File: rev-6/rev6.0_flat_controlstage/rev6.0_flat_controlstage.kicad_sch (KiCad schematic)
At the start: 103 parts, among them J1 PROG, J2 COMM, J3 OSCOPE, J4 PHASE_SIG, J5 ENC_SIG, J6 ANALOG_SIG, J7 POWER, J8 LED, U1 TPS62112, U2 STM32G474RBTx, U3 NCP115ASN330T2G, U4 LM4040C30FTA, U5 LP5900SD-3.3/NOPB, U6 TCAN330, U7 LMV831, Y1 Crystal_GND24

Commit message: Rev 6 pre design review
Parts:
- removed J8: LED, Connector_PinHeader_2.54mm:PinHeader_1x04_P2.54mm_Horizontal, symbol Connector_Generic:Conn_01x04
- removed NT2: NetTie_2, NetTie:NetTie-2_SMD_Pad0.5mm, symbol Device:NetTie_2
- added C52: DNP, Capacitor_SMD:C_0603_1608Metric, symbol Device:C_Small
- added R27, R28: 0, Resistor_SMD:R_0603_1608Metric, symbol Device:R_Small_US
- added TP1, TP10, TP11, TP12, TP13, TP14, TP15, TP16, TP17, TP18, TP19, TP2, TP20, TP21, TP22, TP23, TP24, TP25, TP26, TP27, TP28, TP29, TP3, TP30, TP31, TP4, TP5, TP6, TP7, TP8, TP9: TestPoint_Small, project-footprints:TestPoint_Keystone_5015_Micro-Minature_3DMODEL, symbol Connector:TestPoint_Small
- C12, C13, C14, C16, C17, C18, C20, C22, C23, C25, C27, C28, C31, C32, C34, C44, C45, C46, C48: footprint Capacitor_SMD:C_0603_1608Metric -> Capacitor_SMD:C_0402_1005Metric
- D2, D3, D4: footprint LED_SMD:LED-APA102-2020 -> project-footprints:APA102_2020
- J4: footprint Connector_PinHeader_2.54mm:PinHeader_1x10_P2.54mm_Horizontal -> Connector_PinHeader_2.54mm:PinHeader_2x07_P2.54mm_Horizontal; symbol Connector_Generic:Conn_01x10 -> Connector_Generic:Conn_02x07_Odd_Even
- J5: footprint Connector_PinHeader_2.54mm:PinHeader_1x09_P2.54mm_Horizontal -> Connector_PinHeader_2.54mm:PinHeader_2x06_P2.54mm_Horizontal; symbol Connector_Generic:Conn_01x09 -> Connector_Generic:Conn_02x06_Odd_Even
- J7: footprint Connector_PinHeader_2.54mm:PinHeader_1x03_P2.54mm_Horizontal -> Connector_PinHeader_2.54mm:PinHeader_1x02_P2.54mm_Horizontal; symbol Connector_Generic:Conn_01x03 -> Connector_Generic:Conn_01x02
- R10, R15, R16, R17, R18, R19, R20, R21, R22, R4, R5, R6, R7, R9: footprint Resistor_SMD:R_0603_1608Metric -> Resistor_SMD:R_0402_1005Metric
- R13: value 35.7k -> 35.7k/0.1%
- R14: value 10.2k -> 10.2k/0.1%
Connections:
- net +3V0: now also TP9.1
- net +3V3: now also TP11.1
- net +3V3A: now also TP24.1
- net +5V: now also TP7.1
- net ENC_A: now also J5.3 (Pin_3), TP5.1; no longer J5.2 (Pin_2)
- net ENC_B: now also J5.4 (Pin_4), TP6.1; no longer J5.3 (Pin_3)
- net GND: now also J4.13 (Pin_13), J4.14 (Pin_14), J4.2 (Pin_2), J4.5 (Pin_5), J4.6 (Pin_6), J4.9 (Pin_9), J5.11 (Pin_11), J5.12 (Pin_12), J5.2 (Pin_2), J5.5 (Pin_5), J5.6 (Pin_6), J7.2 (Pin_2), R27.1, TP10.1, TP12.1, TP14.1, TP2.1, TP27.1, TP28.1, TP29.1, TP30.1, TP8.1; no longer J4.4 (Pin_4), J4.7 (Pin_7), J5.4 (Pin_4), J5.9 (Pin_9), J7.1 (Pin_1), J7.3 (Pin_3)
- net PHAH: now also J4.3 (Pin_3); no longer J4.2 (Pin_2)
- net PHAL: now also J4.4 (Pin_4); no longer J4.3 (Pin_3)
- net PHA_SNS_RAW+: now also J6.11 (Pin_11), TP15.1; no longer J6.3 (Pin_3)
- net PHA_SNS_RAW-: now also J6.12 (Pin_12), TP16.1; no longer J6.4 (Pin_4)
- net PHBH: now also J4.7 (Pin_7); no longer J4.5 (Pin_5), U2.38 (PC6)
- net PHBL: now also J4.8 (Pin_8); no longer J4.6 (Pin_6), U2.39 (PC7)
- net PHB_SNS_RAW+: now also TP17.1
- net PHB_SNS_RAW-: now also TP18.1
- net PHCH: now also J4.11 (Pin_11), U2.38 (PC6); no longer J4.8 (Pin_8)
- net PHCL: now also J4.12 (Pin_12), U2.39 (PC7); no longer J4.9 (Pin_9)
- net PHC_SNS_RAW+: now also J6.3 (Pin_3), TP22.1; no longer J6.11 (Pin_11)
- net PHC_SNS_RAW-: now also J6.4 (Pin_4), TP23.1; no longer J6.12 (Pin_12)
- net SPI_MISO: now also J5.8 (Pin_8), TP20.1; no longer J5.6 (Pin_6)
- net SPI_MOSI: now also J5.7 (Pin_7), TP21.1; no longer J5.5 (Pin_5)
- net SPI_SCK: now also J5.10 (Pin_10), TP19.1; no longer J5.7 (Pin_7)
- net SPI_nCS: now also J5.9 (Pin_9), TP26.1; no longer J5.8 (Pin_8)
- net VBUS: now also J7.1 (Pin_1), TP1.1; no longer J7.2 (Pin_2)
- net VBUS_SNS: now also C52.1, R28.2, TP13.1; no longer U7.3 (-), U7.4
- net VBUS_SNS_RAW+: now also TP3.1; no longer C44.2, R15.1, U2.10 (PC2)
- net VBUS_SNS_RAW-: now also TP4.1; no longer C44.1, R16.1, U2.11 (PC3)
- net VREF+: now reaches C12.1, C14.1, C17.1, C8.1, R1.2, U2.28 (VREF+)
- net ENC_A_FLT: now reaches C45.2, R17.1, R19.1, U2.8 (PC0)
- net VDDA: now reaches C25.1, C27.1, C28.1, C29.1, R3.2, U2.29 (VDDA)
- net XTAL_IN: now reaches C9.1, U2.5 (PF0), Y1.3
- net SPI_MISO_FLT: now reaches C48.2, R21.1, R22.1, U2.57 (PB4)
- net STATUS_LED: now reaches D1.1 (K), U2.59 (PB6)
- net XTAL_OUT: now reaches C11.1, U2.6 (PF1), Y1.1
- net ENC_B_FLT: now reaches C46.2, R18.1, R20.1, U2.9 (PC1)
- net EP renamed GNDA
- net GNDA: now also C52.2, R27.2, TP25.1, TP31.1
- new net: R28.1, U7.3 (-), U7.4
- new net VBUS_SNS+: C44.2, R15.1, U2.10 (PC2)
- new net VBUS_SNS-: C44.1, R16.1, U2.11 (PC3)
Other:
- note removed: "Yes I am 50-ohm terminating my SPI lines. Shut up."
- moved on the sheet: C43, JP2, JP3, R13, R14

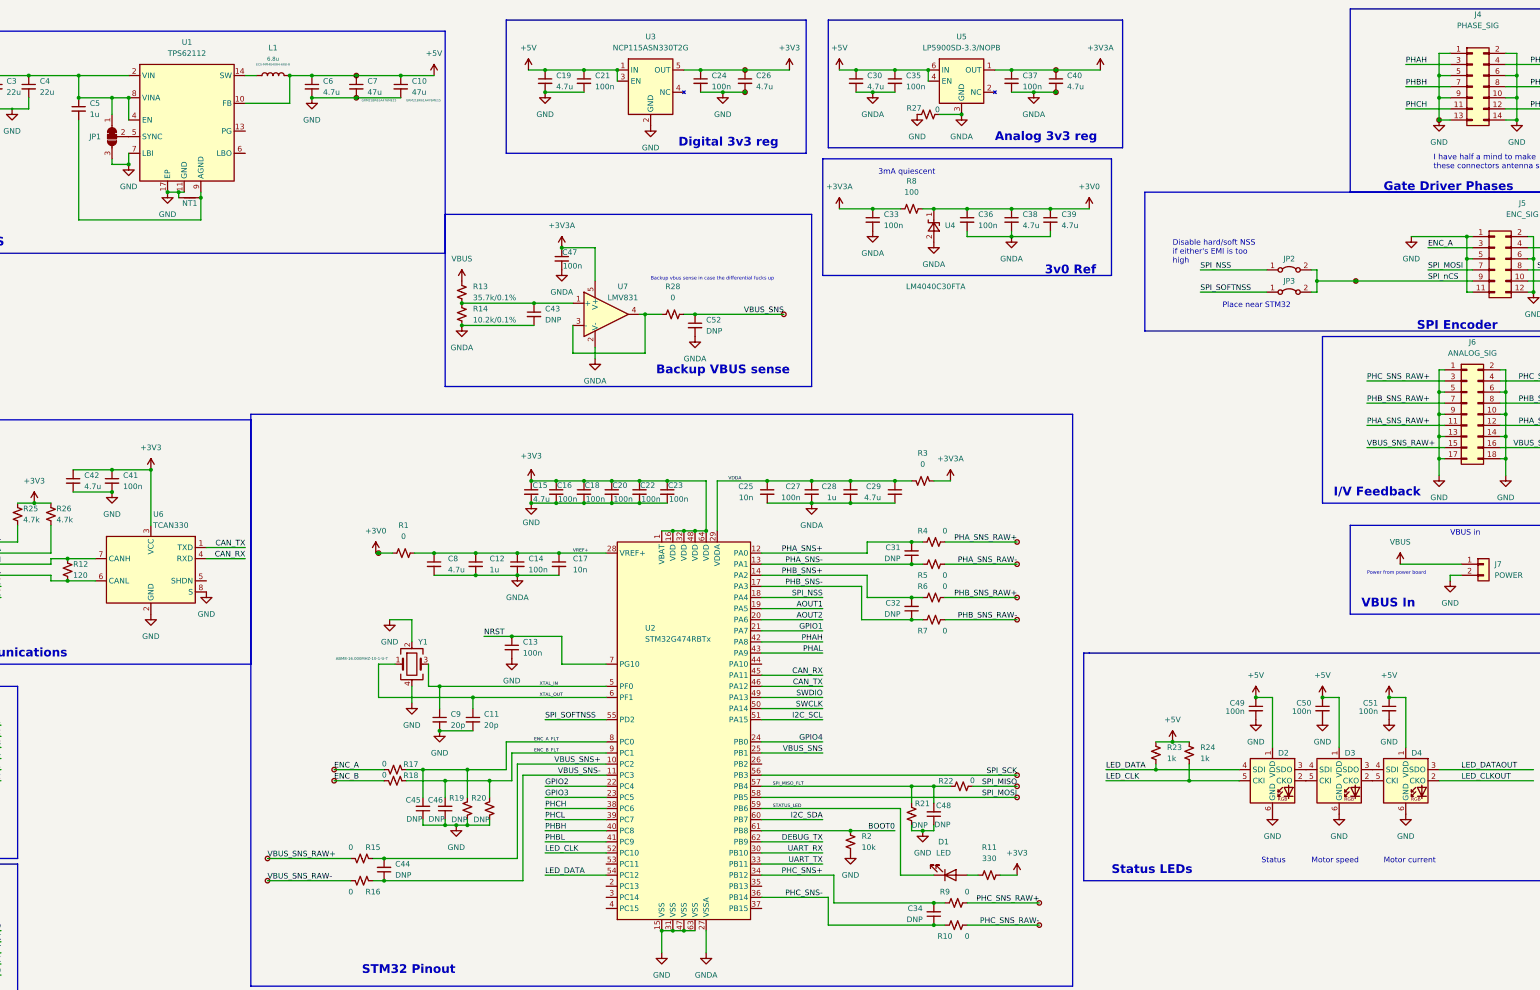
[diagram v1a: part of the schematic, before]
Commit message: Fixed ERC/DRC errors and design rules
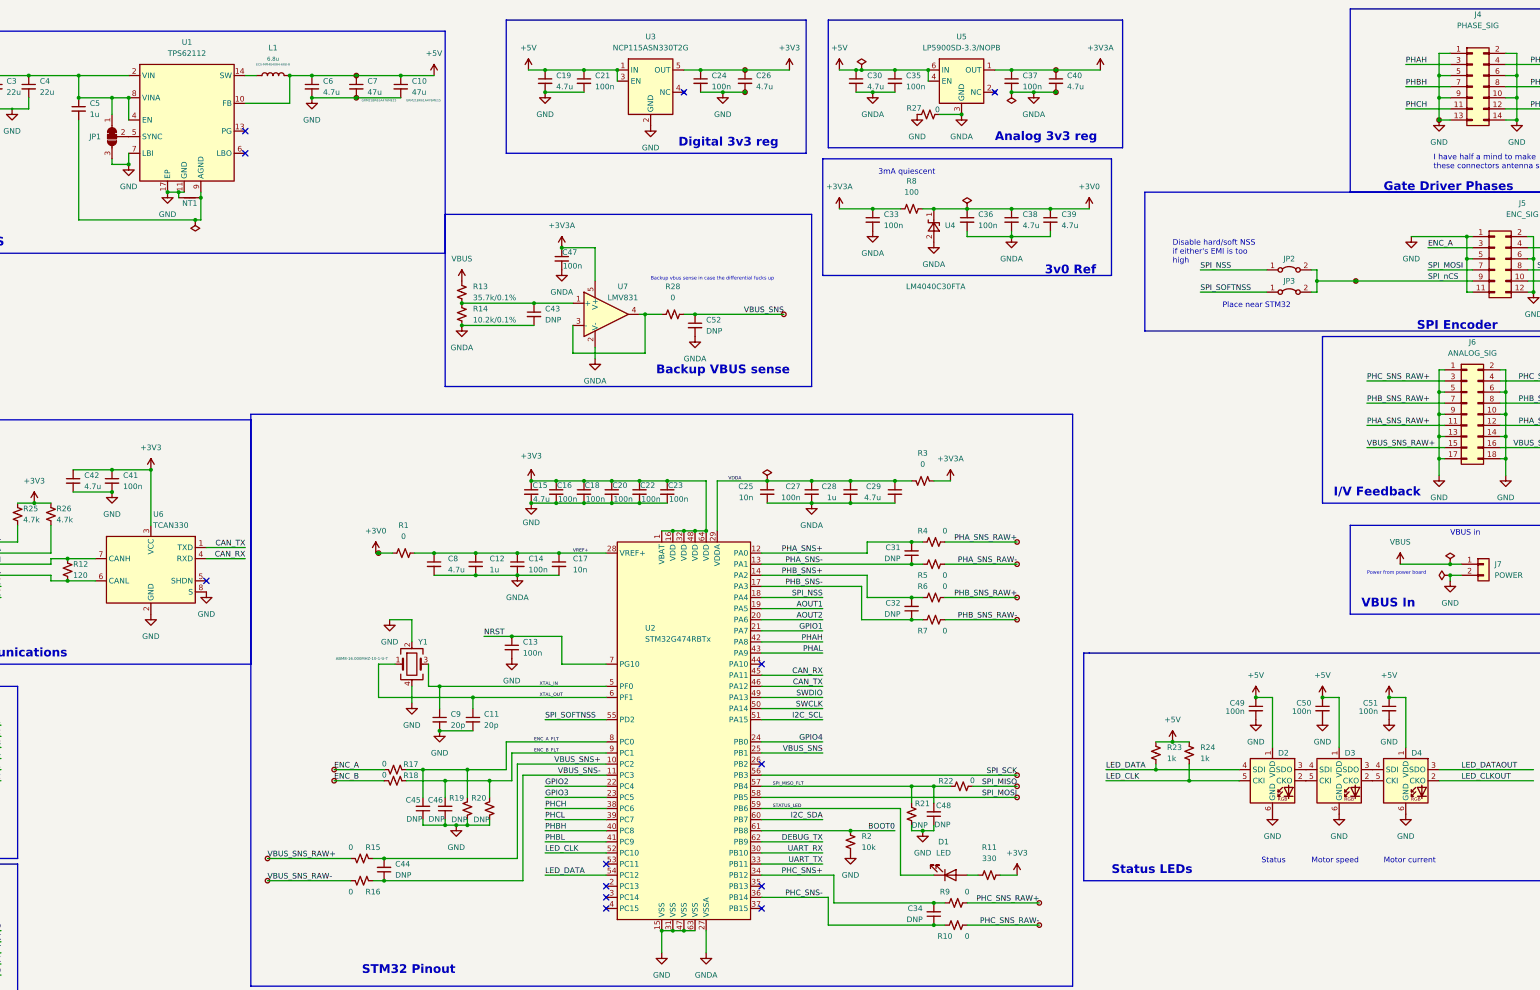
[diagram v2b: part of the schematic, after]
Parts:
- U6: footprint Package_TO_SOT_SMD:SOT-23-8 -> project-footprints:SOT-23-8-Fixed
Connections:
- no-connect marks 0 -> 13

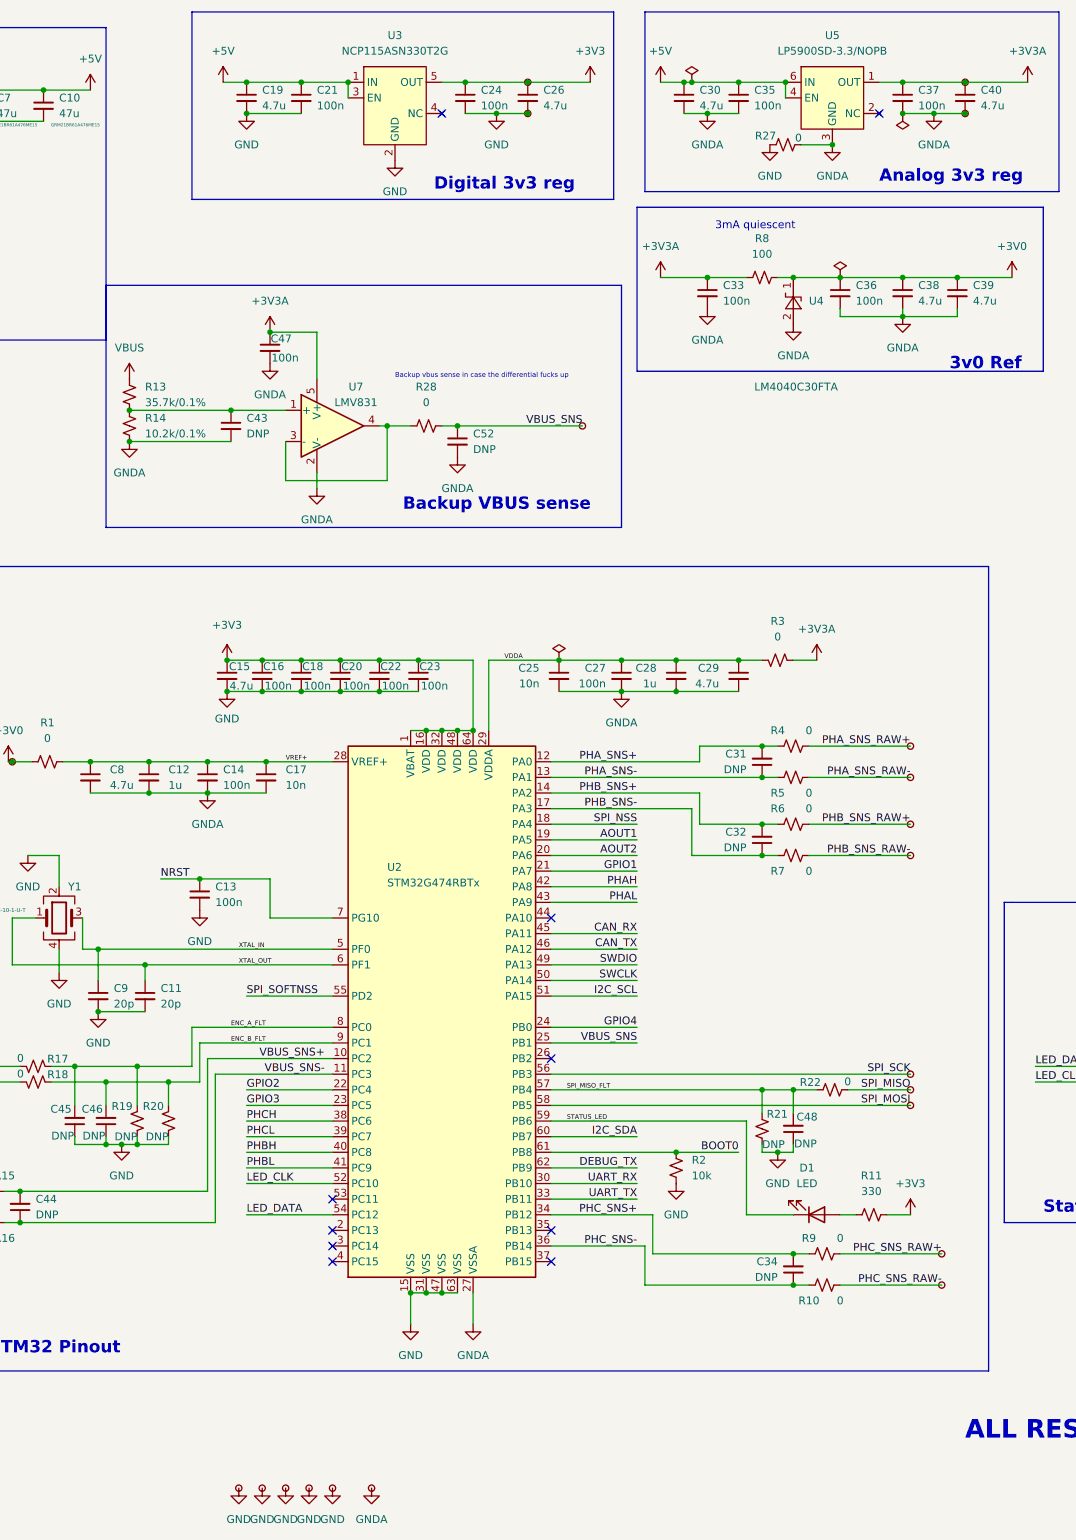
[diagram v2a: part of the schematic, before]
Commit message: Add nonsplit ground version
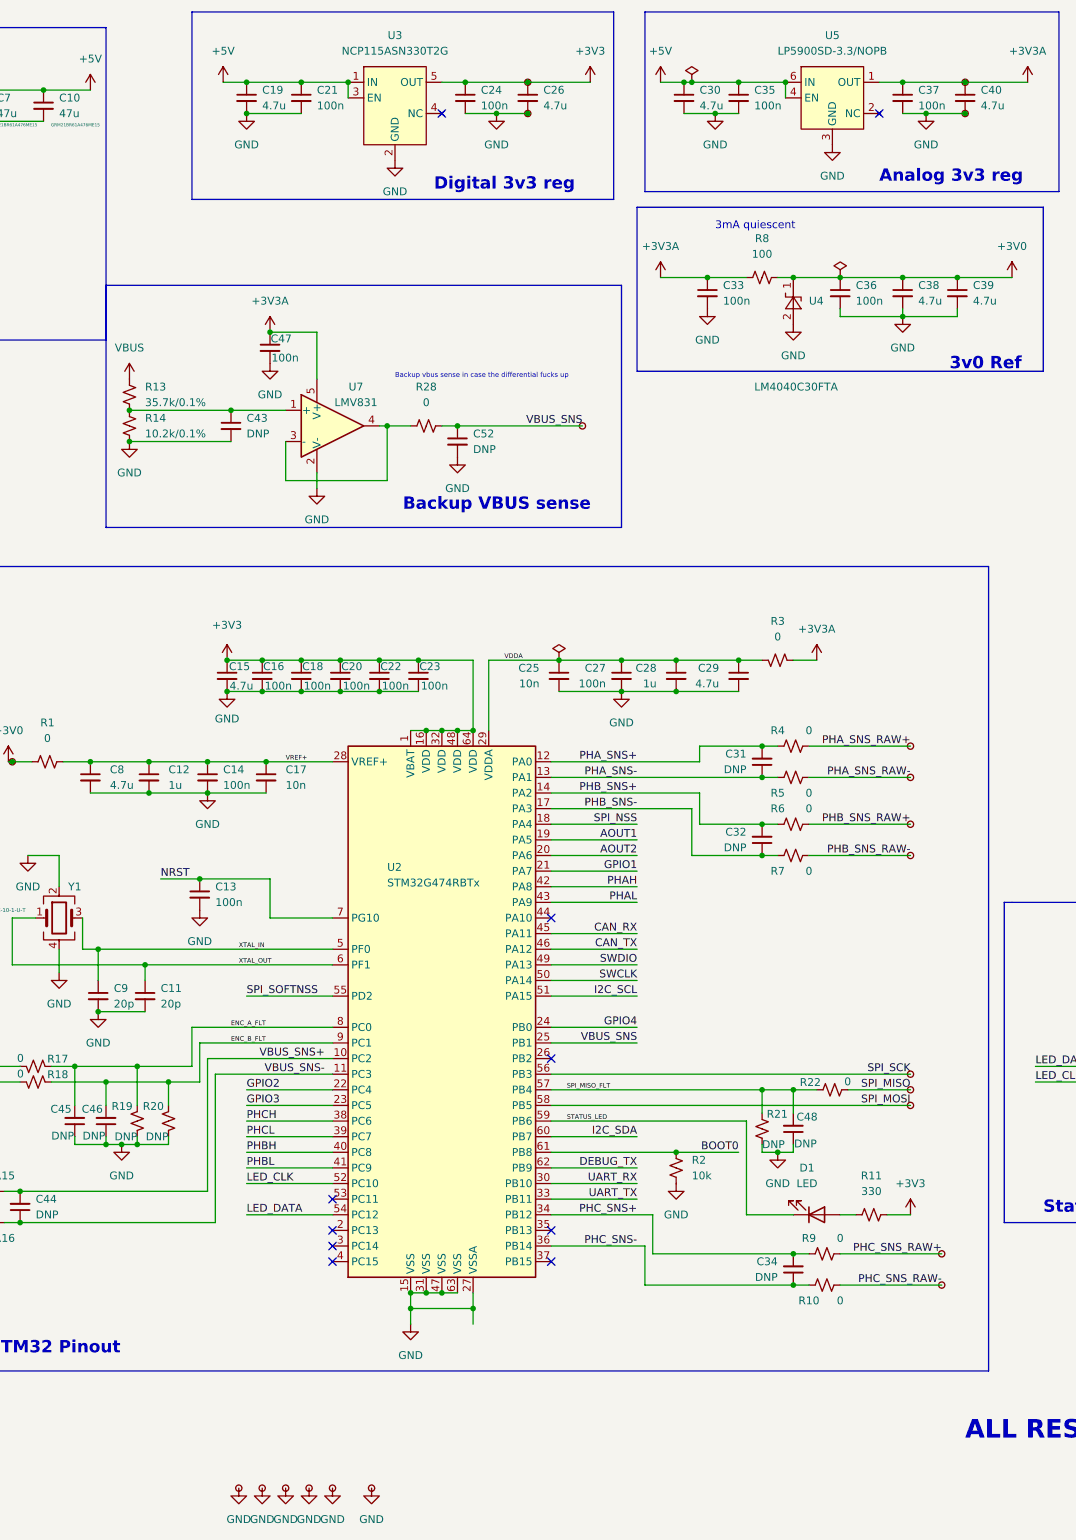
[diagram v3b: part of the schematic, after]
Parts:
- removed R27: 0, Resistor_SMD:R_0603_1608Metric, symbol Device:R_Small_US
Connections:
- net GNDA is gone; now on net GND: C12.2, C14.2, C17.2, C25.2, C27.2, C28.2, C29.2, C30.2, C33.2, C35.2, C36.2, C37.2, C38.2, C39.2, C40.2, C43.2, C47.2, C52.2, C8.2, R14.2, TP25.1, TP31.1, U2.27 (VSSA), U4.2 (A), U5.3 (GND), U5.7 (GND), U7.2 (V-)
